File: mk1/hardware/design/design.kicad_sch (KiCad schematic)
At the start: 30 parts, among them U1 Teensy4.1, U10 LIS2MDL, U2 HM-TRP-868, U3 BMP390, U4 LSM6DSV80X, U5 D30V30MAL, U6 L80-R, U7 VN5E160STR, U8 VN5E160STR

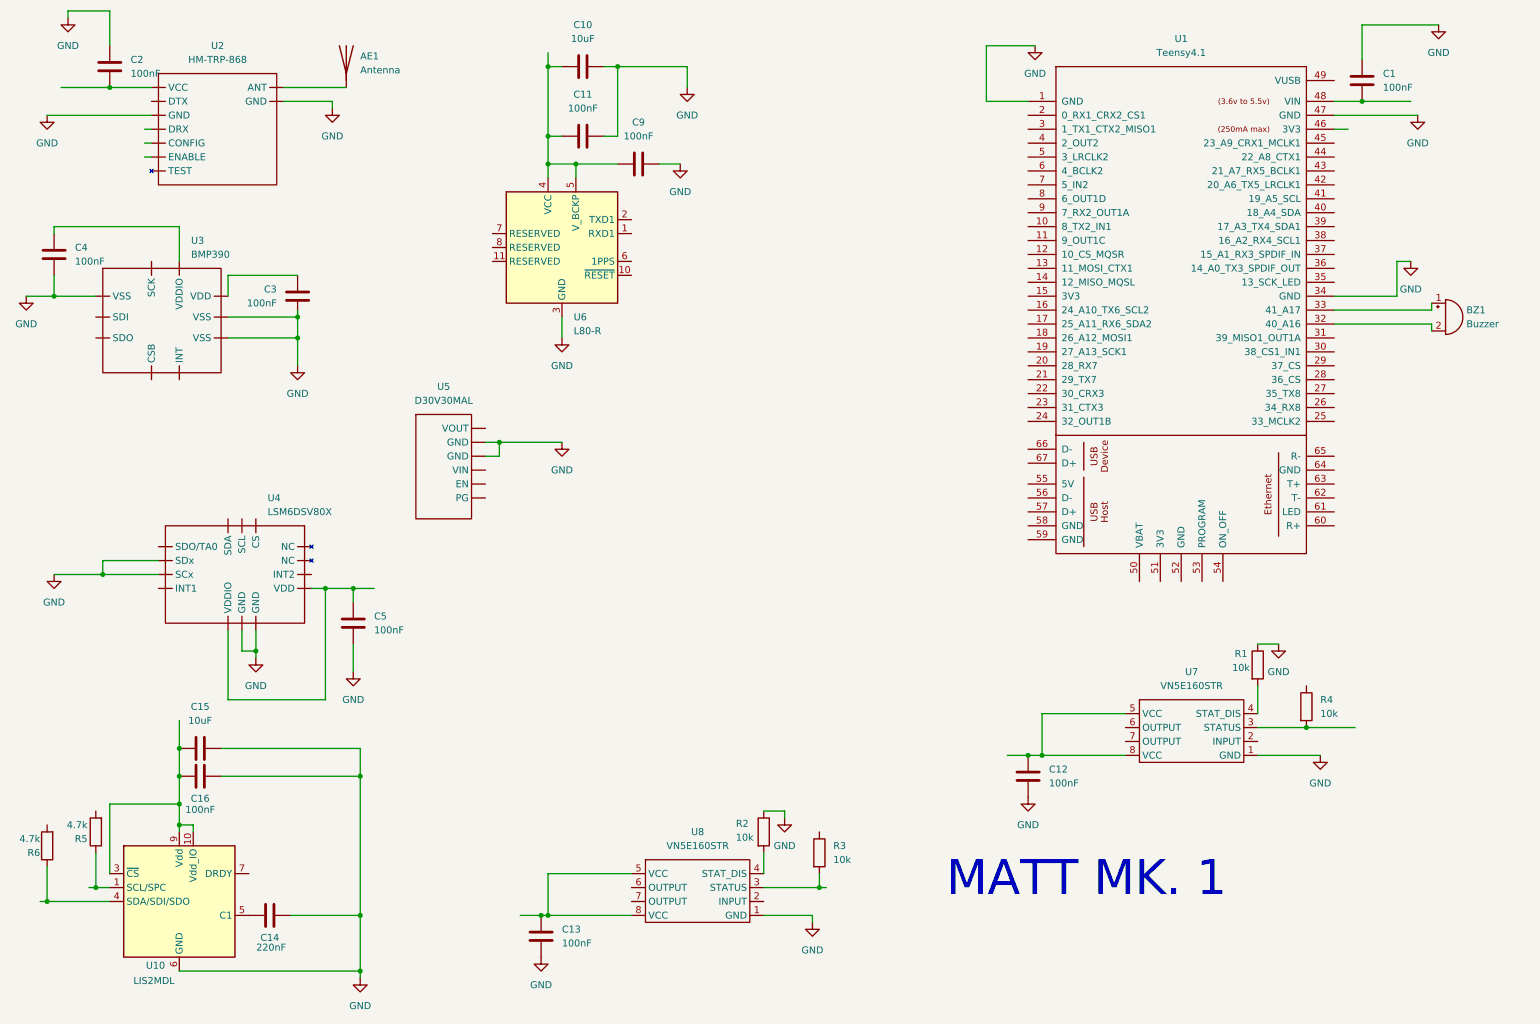
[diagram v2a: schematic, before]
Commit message: Added footprints
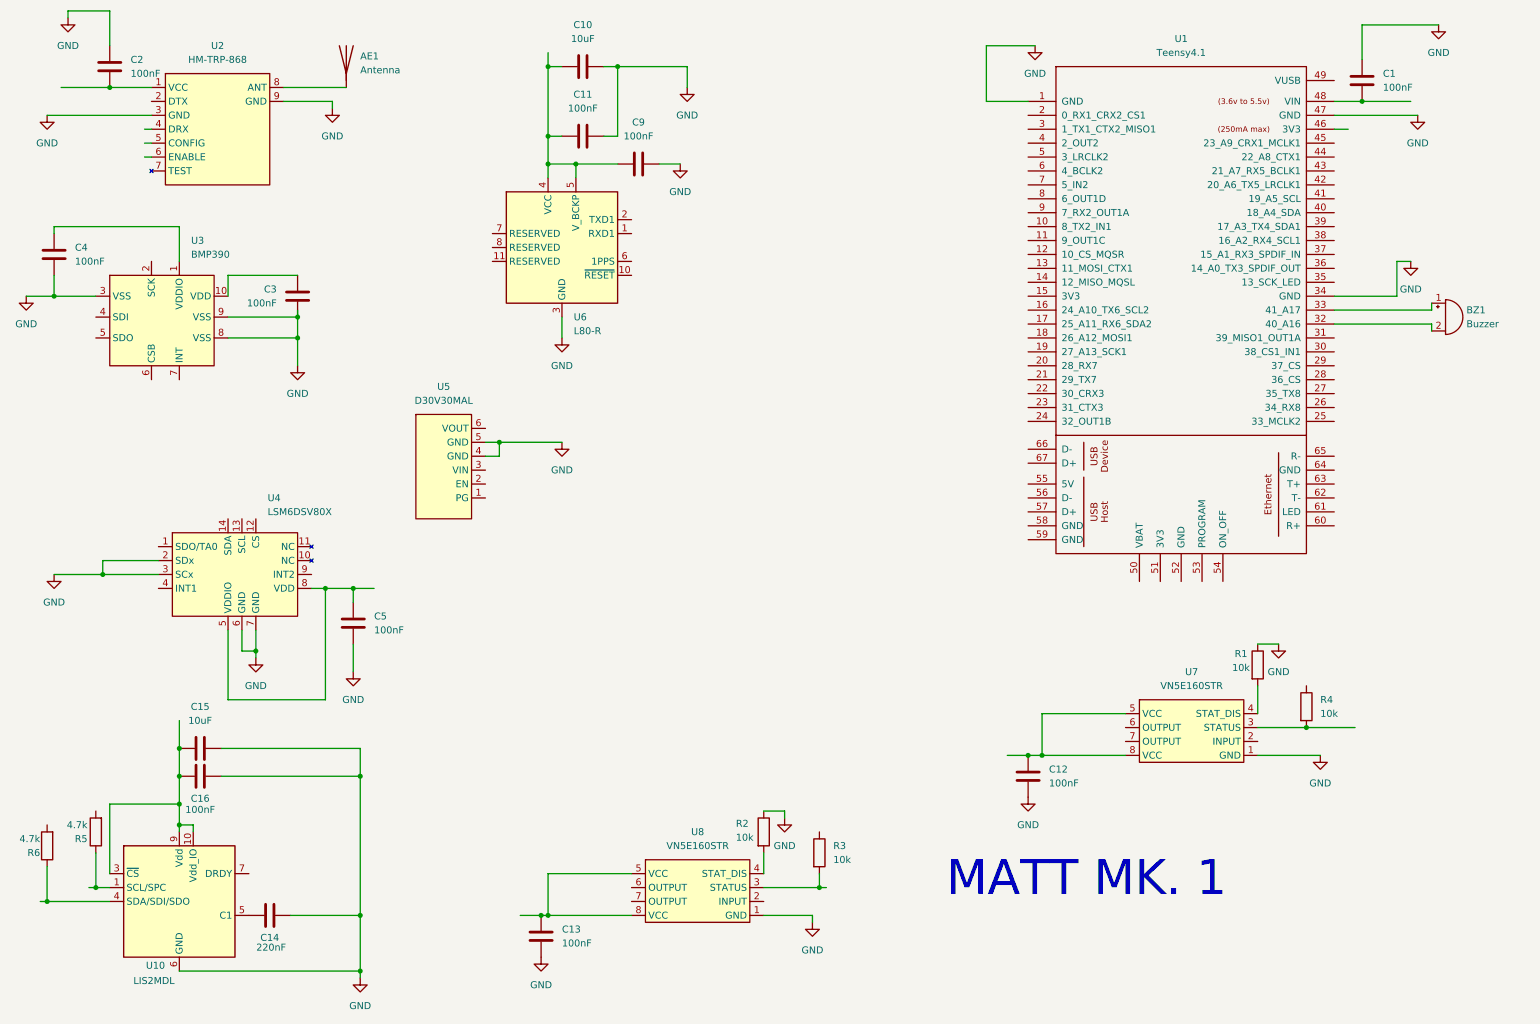
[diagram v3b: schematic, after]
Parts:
- U1: footprint (none) -> missing_footprints:teensy4.1
- U2: footprint (none) -> missing_footprints:HM-TRP-XXX
- U3: footprint (none) -> missing_footprints:BMP390
- U4: footprint (none) -> missing_footprints:LSM6DSV80X
- U5: footprint (none) -> missing_footprints:D30V30MAx
- U7, U8: footprint (none) -> missing_footprints:vn5e160s
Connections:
- net GND: now also U2.3 (GND), U2.9 (GND), U3.3 (VSS), U3.8 (VSS), U3.9 (VSS), U4.2 (SDx), U4.3 (SCx), U4.6 (GND), U4.7 (GND), U5.4 (GND), U5.5 (GND); no longer U2. (GND), U3. (VSS), U4. (VDD), U5. (PG)
- net at C5.1: now also U4.5 (VDDIO), U4.8 (VDD); no longer U4. (VDD)
- net at C2.2: now also U2.1 (VCC); no longer U2. (GND)
- net at AE1.1 (A): now also U2.8 (ANT); no longer U2. (GND)
- net at C4.1: now also U3.1 (VDDIO); no longer U3. (VSS)
- net at C3.1: now also U3.10 (VDD); no longer U3. (VSS)
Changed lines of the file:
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@@
 			)
 		)
-		(property "Footprint" ""
+		(property "Footprint" "missing_footprints:teensy4.1"
 			(at 215.9 76.2 0)
 			(effects
@@
 			)
 		)
-		(property "Datasheet" ""
+		(property "Datasheet" "https://www.pjrc.com/store/teensy41.html"
 			(at 215.9 76.2 0)
 			(effects
@@
 			)
 		)
-		(property "Description" ""
+		(property "Description" "The microcontroller"
 			(at 226.06 86.36 0)
 			(effects
@@
 	)
 	(symbol
+		(lib_name "VN5E160STR_1")
 		(lib_id "rockety_extras:VN5E160STR")
 		(at 137.16 176.53 0)
@@
 			)
 		)
-		(property "Footprint" ""
+		(property "Footprint" "missing_footprints:vn5e160s"
 			(at 137.16 176.53 0)
 			(effects
@@
 			)
 		)
-		(property "Datasheet" ""
+		(property "Datasheet" "https://www.st.com/resource/en/datasheet/vn5e160s-e.pdf"
 			(at 137.16 176.53 0)
 			(effects
@@
 			)
 		)
-		(property "Description" ""
+		(property "Description" "High side driver for deployment charges"
 			(at 137.16 176.53 0)
 			(effects
@@
 			)
 		)
-		(property "Footprint" ""
+		(property "Footprint" "missing_footprints:LSM6DSV80X"
 			(at 48.26 114.3 0)
 			(effects
@@
 			)
 		)
-		(property "Datasheet" ""
+		(property "Datasheet" "https://www.st.com/resource/en/datasheet/lsm6dsv80x.pdf"
 			(at 48.26 114.3 0)
 			(effects
@@
 			)
 		)
-		(property "Description" ""
+		(property "Description" "Accelerometers and Gyroscopes"
 			(at 48.26 114.3 0)
 			(effects
@@
 			)
 		)
-		(pin ""
-		)
-		(pin ""
-		)
-		(pin ""
-		)
-		(pin ""
-		)
-		(pin ""
-		)
-		(pin ""
-		)
-		(pin ""
-		)
-		(pin ""
-		)
-		(pin ""
-		)
-		(pin ""
-		)
-		(pin ""
-		)
-		(pin ""
-		)
-		(pin ""
-		)
-		(pin ""
+		(pin "2"
+		)
+		(pin "7"
+		)
+		(pin "11"
+		)
+		(pin "3"
+		)
+		(pin "12"
+		)
+		(pin "1"
+		)
+		(pin "4"
+		)
+		(pin "14"
+		)
+		(pin "8"
+		)
+		(pin "6"
+		)
+		(pin "10"
+		)
+		(pin "13"
+		)
+		(pin "9"
+		)
+		(pin "5"
 		)
 		(instances
@@
 			)
 		)
-		(property "Footprint" ""
+		(property "Footprint" "missing_footprints:HM-TRP-XXX"
 			(at 45.72 33.02 0)
 			(effects
@@
 			)
 		)
-		(property "Datasheet" ""
+		(property "Datasheet" "https://www.tme.eu/Document/34c5f8a4794dad7a5068931b0a0d37c0/HM-TRP-869S.pdf"
 			(at 45.72 33.02 0)
 			(effects
@@
 			)
 		)
-		(property "Description" ""
+		(property "Description" "Radio module"
 			(at 45.72 33.02 0)
 			(effects
@@
 			)
 		)
-		(pin ""
-		)
-		(pin ""
-		)
-		(pin ""
-		)
-		(pin ""
-		)
-		(pin ""
-		)
-		(pin ""
-		)
-		(pin ""
-		)
-		(pin ""
-		)
-		(pin ""
+		(pin "6"
+		)
+		(pin "7"
+		)
+		(pin "8"
+		)
+		(pin "9"
+		)
+		(pin "1"
+		)
+		(pin "2"
+		)
+		(pin "3"
+		)
+		(pin "4"
+		)
+		(pin "5"
 		)
 		(instances
@@
 			)
 		)
-		(property "Footprint" ""
+		(property "Footprint" "missing_footprints:BMP390"
 			(at 39.37 69.85 0)
 			(effects
@@
 			)
 		)
-		(property "Datasheet" ""
+		(property "Datasheet" "https://www.mouser.co.uk/datasheet/3/1046/1/bst_bmp390_ds002.pdf"
 			(at 39.37 69.85 0)
 			(effects
@@
 			)
 		)
-		(property "Description" ""
+		(property "Description" "Pressure sensor"
 			(at 39.37 69.85 0)
 			(effects
@@
 			)
 		)
-		(pin ""
-		)
-		(pin ""
-		)
-		(pin ""
-		)
-		(pin ""
-		)
-		(pin ""
-		)
-		(pin ""
-		)
-		(pin ""
-		)
-		(pin ""
-		)
-		(pin ""
-		)
-		(pin ""
+		(pin "1"
+		)
+		(pin "4"
+		)
+		(pin "2"
+		)
+		(pin "10"
+		)
+		(pin "5"
+		)
+		(pin "6"
+		)
+		(pin "7"
+		)
+		(pin "8"
+		)
+		(pin "3"
+		)
+		(pin "9"
 		)
 		(instances
@@
 			)
 		)
-		(property "Footprint" ""
+		(property "Footprint" "missing_footprints:vn5e160s"
 			(at 227.33 147.32 0)
 			(effects
@@
 			)
 		)
-		(property "Datasheet" ""
+		(property "Datasheet" "https://www.st.com/resource/en/datasheet/vn5e160s-e.pdf"
 			(at 227.33 147.32 0)
 			(effects
@@
 			)
 		)
-		(property "Description" ""
+		(property "Description" "High side driver for deployment charges"
 			(at 227.33 147.32 0)
 			(effects
@@
 			)
 		)
-		(property "Footprint" ""
+		(property "Footprint" "missing_footprints:D30V30MAx"
 			(at 88.9 95.25 0)
 			(effects
@@
 			)
 		)
-		(property "Datasheet" ""
+		(property "Datasheet" "https://www.pololu.com/file/0J2035/d30v30max-fine-adjust-step-down-voltage-regulator-dimensions.pdf"
 			(at 88.9 95.25 0)
 			(effects
@@
 			)
 		)
-		(property "Description" ""
+		(property "Description" "Variable voltage regulator"
 			(at 88.9 95.25 0)
 			(effects
@@
 			)
 		)
-		(pin ""
-		)
-		(pin ""
-		)
-		(pin ""
-		)
-		(pin ""
-		)
-		(pin ""
-		)
-		(pin ""
-		)
-		(instances
+		(pin "1"
+		)
+		(pin "2"
+		)
+		(pin "3"
+		)
+		(pin "5"
+		)
+		(pin "4"
+		)
+		(pin "6"
+		)
+		(instances

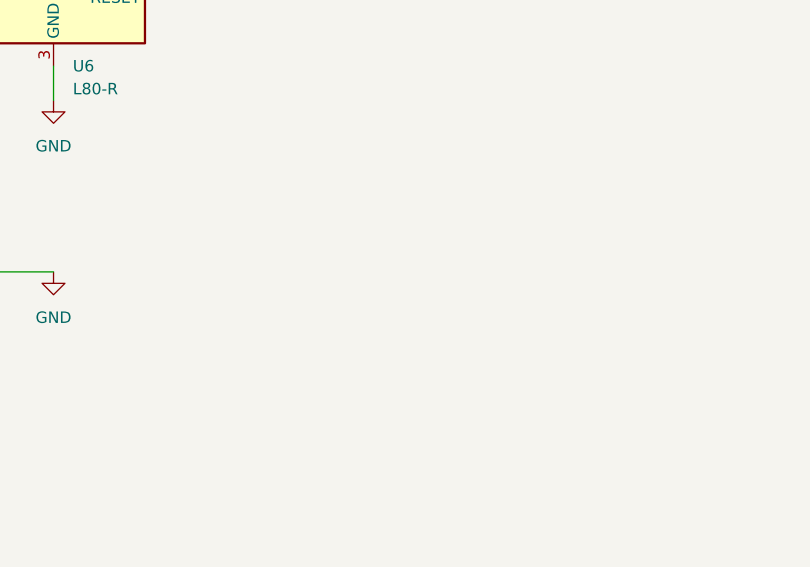
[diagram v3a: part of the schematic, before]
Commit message: Add BOM and make a start at giving everything a suitable footprint
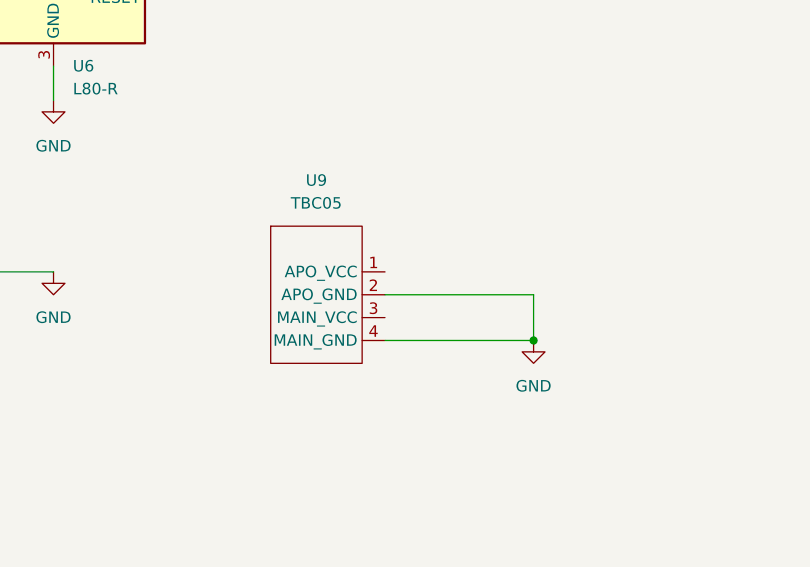
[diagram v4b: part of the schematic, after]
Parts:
- added U9: TBC05, symbol missing_chips:TBC05_04
- BZ1: footprint (none) -> missing_footprints:AX1203DLF
- C1, C10, C11, C12, C13, C14, C15, C16, C2, C3, C4, C5, C9: footprint (none) -> Capacitor_SMD:C_0805_2012Metric_Pad1.18x1.45mm_HandSolder
- R1, R2, R3, R4, R5, R6: footprint (none) -> Resistor_SMD:R_0805_2012Metric_Pad1.20x1.40mm_HandSolder
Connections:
- net GND: now also U9.2 (APO_GND), U9.4 (MAIN_GND)

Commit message: Picked antenna for BOM and added footprint
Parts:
- AE1: footprint (none) -> missing_footprints:ANT-868-PW
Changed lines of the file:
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@@
 			)
 		)
-		(property "Footprint" ""
+		(property "Footprint" "missing_footprints:ANT-868-PW"
 			(at 73.66 24.13 0)
 			(effects
@@
 			)
 		)
-		(property "Datasheet" "~"
+		(property "Datasheet" "https://www.te.com/commerce/DocumentDelivery/DDEController?Action=srchrtrv&DocNm=ANT-868-PW-LP&DocType=Data+Sheet&DocLang=English&DocFormat=pdf&PartCntxt=ANT-868-PW-LP"
 			(at 73.66 24.13 0)
 			(effects

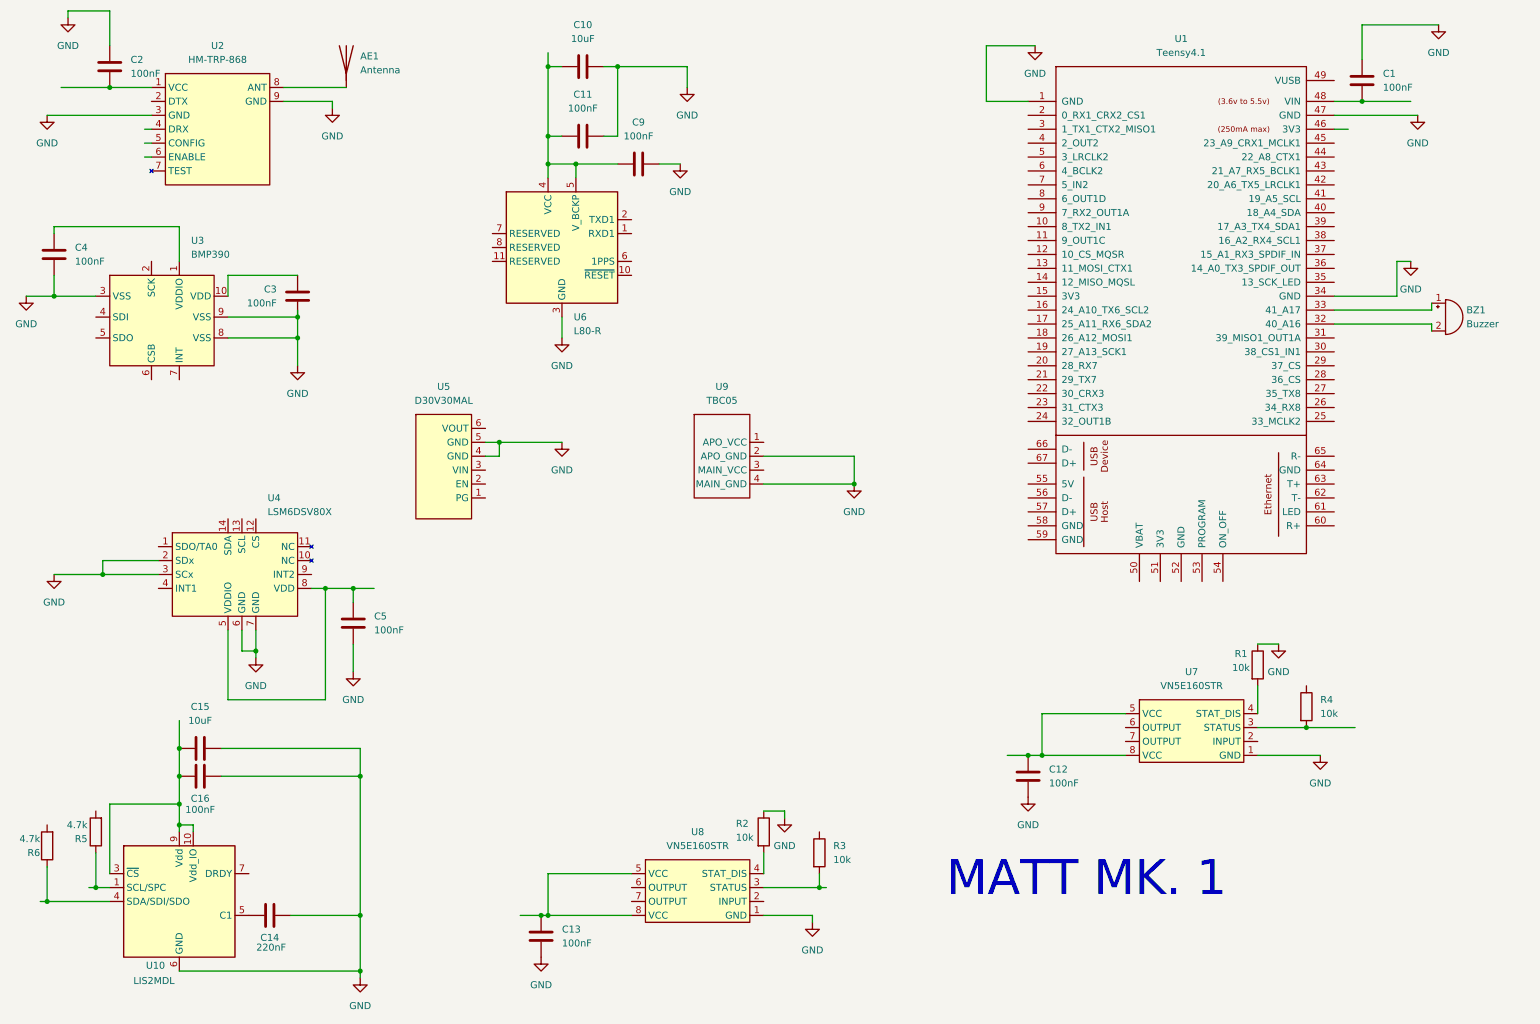
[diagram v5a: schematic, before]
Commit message: Add a few missing in and outputs, try to join up pins
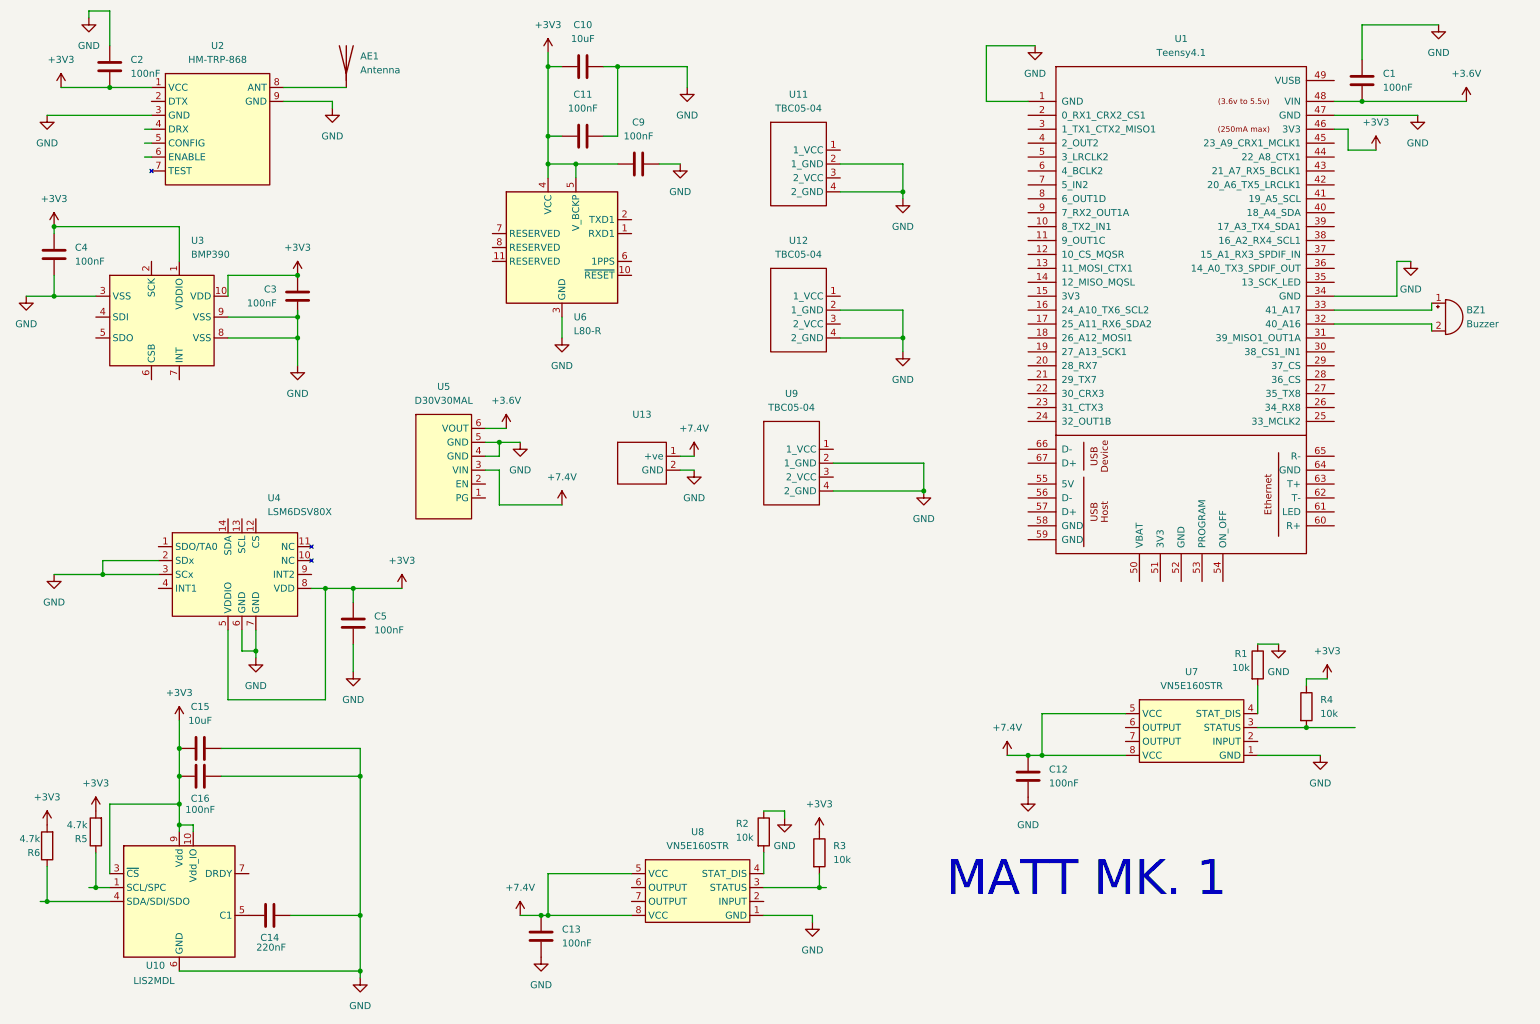
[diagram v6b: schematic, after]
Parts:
- added U11: TBC05-04, missing_footprints:TBC05-04_pwm1, symbol missing_chips:TBC05_04
- added U12: TBC05-04, missing_footprints:TBC05-04_pwm2, symbol missing_chips:TBC05_04
- added U13: ~, missing_footprints:power_in, symbol missing_chips:power_in
- U9: value TBC05 -> TBC05-04; footprint (none) -> missing_footprints:TBC05-04_charges
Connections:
- net GND: now also U11.2 (1_GND), U11.4 (2_GND), U12.2 (1_GND), U12.4 (2_GND), U13.2 (GND)
- net +3V3: now reaches U1.46 (3V3)
- net +3V3: now also C10.2, C11.2, C15.1, C16.2, C2.2, C3.1, C4.1, C5.1, C9.2, R3.1, R4.1, R5.2, R6.2, U10.10 (Vdd_IO), U10.3 (~{CS}), U10.9 (Vdd), U2.1 (VCC), U3.1 (VDDIO), U3.10 (VDD), U4.5 (VDDIO), U4.8 (VDD), U6.4 (VCC), U6.5 (V_BCKP)
- net +3.6V: now reaches C1.1, U1.48 (VIN)
- net +3.6V: now also U5.6 (VOUT)
- net +7.4V: now reaches C13.1, U8.5 (VCC), U8.8 (VCC)
- net +7.4V: now also C12.1, U5.3 (VIN), U7.5 (VCC), U7.8 (VCC), U13.1 (+ve)
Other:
- moved on the sheet: U9
